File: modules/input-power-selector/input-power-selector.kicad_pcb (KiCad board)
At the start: 2 copper layers, 61 x 45.6 mm, 37 parts, among them Q1 SI4909DY-T1-GE3, Q2 SI4909DY-T1-GE3, Q3 SI4909DY-T1-GE3, Q4 IPF067N20NM6ATMA1, Q7 BC847, U1 LTC4417IGN, U2 SQJQ141EL-T1_GE3

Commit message: add missing footprints and symbols
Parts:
- M2: footprint MegaCastle:MegaCastle2x24-Module-I42.0x56.2-M88887D8C0001 -> MegaCastle:MegaCastle2x24-Module-I42.0x56.2-M88887D8C0001-NIBBLE
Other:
- board size 61 x 45.6 mm -> 61 x 48.8 mm
- board text added: "Power Input Selector Module R20250405 github.com/mega65/ megaphone-modular"
- board text added: "Power Input Selector Module R20250405 github.com/mega65/megaphone-modular"
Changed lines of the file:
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@@
 			(outputformat 1)
 			(mirror no)
-			(drillshape 1)
+			(drillshape 0)
 			(scaleselection 1)
-			(outputdirectory "")
+			(outputdirectory "gerbers/")
 		)
 	)
@@
 	(net 30 "Net-(U2-G)")
 	(net 31 "unconnected-(M2-VCC-Pad1)")
-	(footprint "MegaCastle:MegaCastle2x24-Module-I42.0x56.2-M88887D8C0001"
+	(footprint "MegaCastle:MegaCastle2x24-Module-I42.0x56.2-M88887D8C0001-NIBBLE"
 		(layer "F.Cu")
 		(at 52.451 42.485 90)
@@
 			)
 		)
-		(property "Footprint" "MegaCastle:MegaCastle2x24-Module-I42.0x56.2-M88887D8C0001"
+		(property "Footprint" "MegaCastle:MegaCastle2x24-Module-I42.0x56.2-M88887D8C0001-NIBBLE"
 			(at 0 0 90)
 			(layer "F.Fab")
@@
 		)
 		(fp_line
-			(start 22.799999 -30.48)
-			(end 22.799999 30.48)
+			(start 24.387499 -30.48)
+			(end 24.387499 30.48)
 			(stroke
 				(width 0.05)
@@
 		)
 		(fp_line
-			(start -22.799999 -30.48)
-			(end 22.799999 -30.48)
+			(start -24.387499 -30.48)
+			(end 24.387499 -30.48)
 			(stroke
 				(width 0.05)
@@
 		)
 		(fp_line
-			(start -22.799999 -30.48)
-			(end -22.799999 30.48)
+			(start -24.387499 -30.48)
+			(end -24.387499 30.48)
 			(stroke
 				(width 0.05)
@@
 		)
 		(fp_text user "PRY"
-			(at 0 -29.18 90)
+			(at 0 30.18 90)
 			(unlocked yes)
 			(layer "B.SilkS")
@@
 		)
 		(fp_text user "PRY"
-			(at 0 30.18 90)
+			(at 0 -29.18 90)
 			(unlocked yes)
 			(layer "B.SilkS")
@@
 		)
 	)
+	(gr_text "Power Input Selector Module\nR20250405\ngithub.com/mega65/\nmegaphone-modular"
+		(at 46.609 60.96 0)
+		(layer "B.SilkS")
+		(effects
+			(font
+				(size 1 1)
+				(thickness 0.1)
+			)
+			(justify left bottom mirror)
+		)
+	)
 	(gr_text "Reverse\nPolarity\nProtection\nBypass"
 		(at 38.2862 50.0362 -0)
@@
 		)
 	)
-	(gr_text "IPF067N20NM6ATMA1"
-		(at 55.609 31.164 -0)
+	(gr_text "Power Input Selector Module\nR20250405\ngithub.com/mega65/megaphone-modular"
+		(at 24.638 61.087 0)
 		(layer "F.SilkS")
 		(effects
 			(font
 				(size 1 1)
-				(thickness 0.15)
+				(thickness 0.1)
 			)
 			(justify left bottom)
 		)
 	)
-	(dimension
-		(type aligned)
-		(layer "Dwgs.User")
-		(pts
-			(xy 74.532 21.766) (xy 74.532 63.676)
-		)
-		(height 31.75)
-		(gr_text "41.9100 mm"
-			(at 41.632 42.721 90)
-			(layer "Dwgs.User")
-			(effects
-				(font
-					(size 1 1)
-					(thickness 0.15)
-				)
-			)
-		)
-		(format
-			(prefix "")
-			(suffix "")
-			(units 3)
-			(units_format 1)
-			(precision 4)
-		)
-		(style
-			(thickness 0.1)
-			(arrow_length 1.27)
-			(text_position_mode 0)
-			(extension_height 0.58642)
-			(extension_offset 0.5) keep_text_aligned)
-	)
-	(dimension
-		(type aligned)
-		(layer "Dwgs.User")
-		(pts
-			(xy 24.765 30.3322) (xy 80.01 30.3322)
-		)
-		(height 33.655)
-		(gr_text "55.2450 mm"
-			(at 52.3875 62.8372 0)
-			(layer "Dwgs.User")
-			(effects
-				(font
-					(size 1 1)
-					(thickness 0.15)
-				)
+	(gr_text "IPF067N20NM6ATMA1"
+		(at 55.609 31.164 -0)
+		(layer "F.SilkS")
+		(effects
+			(font
+				(size 1 1)
+				(thickness 0.15)
 			)
+			(justify left bottom)
 		)
-		(format
-			(prefix "")
-			(suffix "")
-			(units 3)
-			(units_format 1)
-			(precision 4)
-		)
-		(style
-			(thickness 0.1)
-			(arrow_length 1.27)
-			(text_position_mode 0)
-			(extension_height 0.58642)
-			(extension_offset 0.5) keep_text_aligned)
 	)
 	(segment

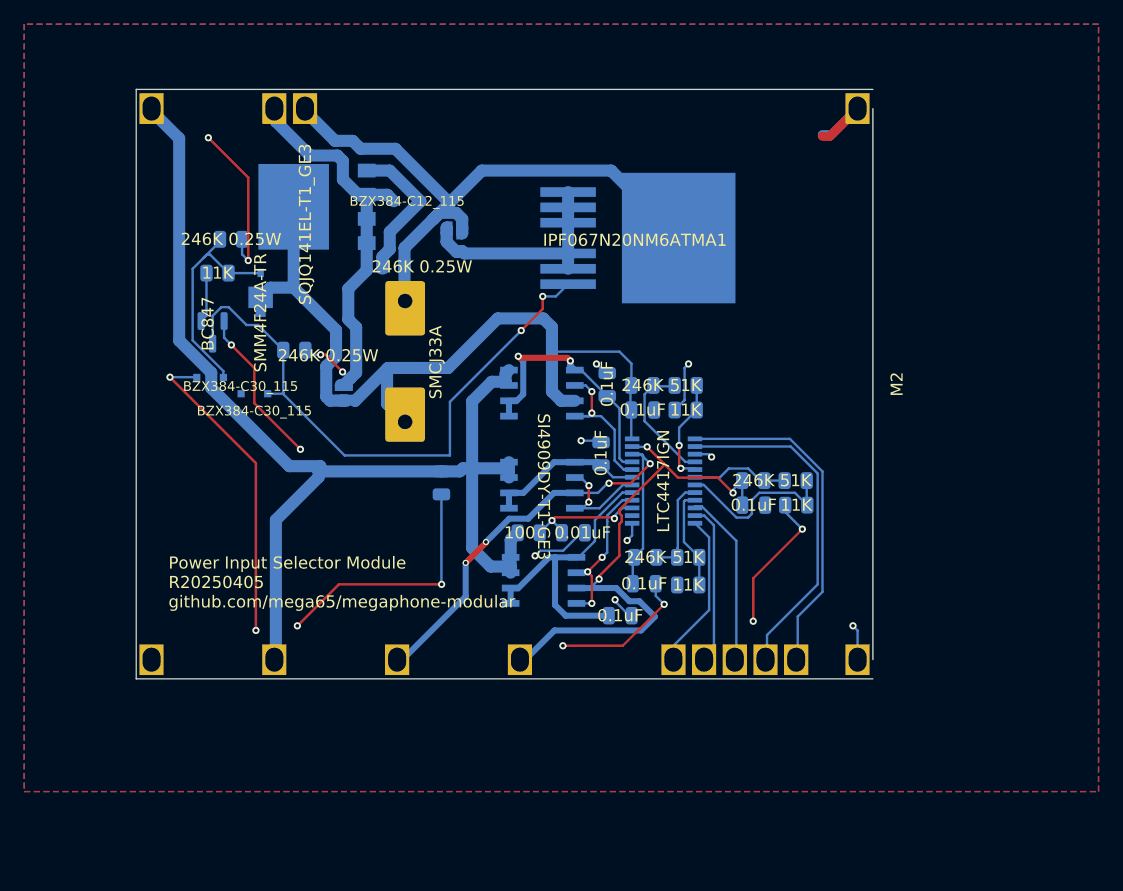
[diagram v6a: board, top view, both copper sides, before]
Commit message: Updating footprint on input power selector
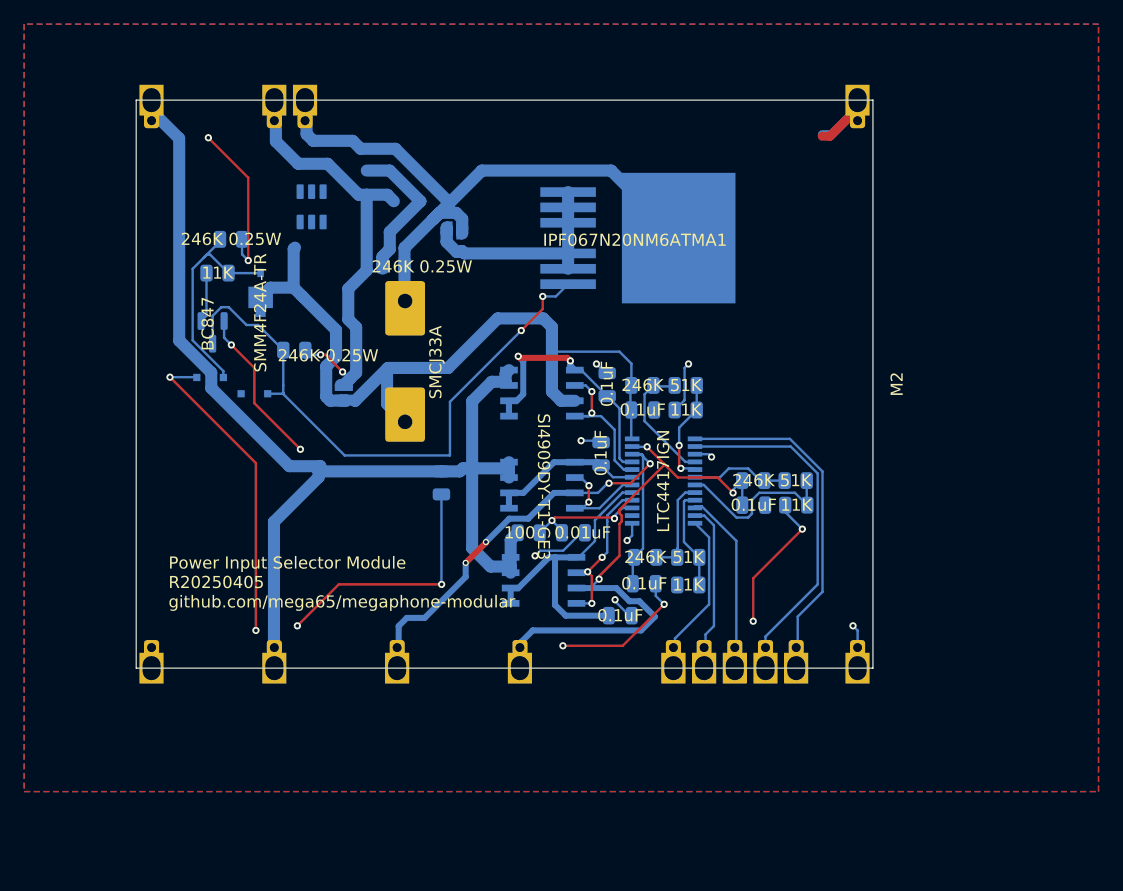
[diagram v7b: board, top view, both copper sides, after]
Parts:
- D1, D2, D3: footprint footprints:DIO_BZX384-C30_115 -> MegaCastle:DIO_BZX384-C30_115
- M2: footprint MegaCastle:MegaCastle2x24-Module-I42.0x56.2-M88887D8C0001-NIBBLE -> MegaCastle:MegaCastle2x24-Module-I47.0x56.2-M88887D8C0001-SPAREPAD
- U2: footprint footprints:PowerPAK_8x8L_BWL-2_VIS -> MegaCastle:SOT95P280X120-6N
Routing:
- net DIRTY_DC_+_PROTECTED: track 67.7 -> 64.3 mm
- net DIRTY_DC_-: track 50.8 -> 51.8 mm
- net INTERNAL_SOLAR_IN: track 46.7 -> 47.8 mm
- net USB-C_POWER_IN: track 43.0 -> 43.9 mm
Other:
- board size 61 x 48.8 mm -> 61 x 47 mm
